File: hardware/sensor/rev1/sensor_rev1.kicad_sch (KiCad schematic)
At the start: 4 parts

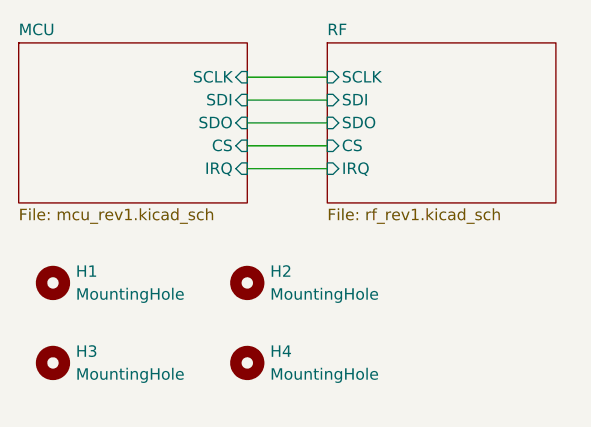
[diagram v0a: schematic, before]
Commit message: EG-49 Board size and mounting holes placed.
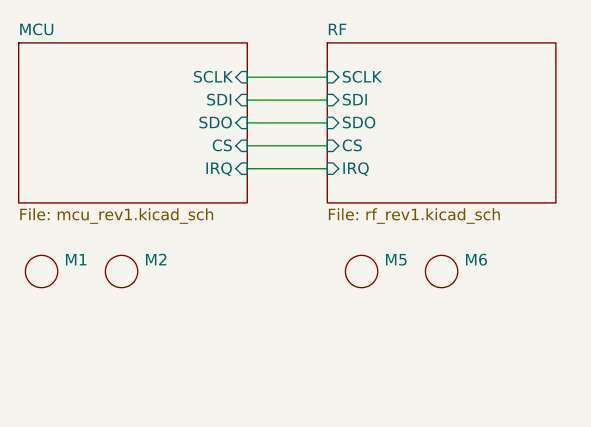
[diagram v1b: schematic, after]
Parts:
- removed H1, H2, H3, H4: MountingHole, MountingHole:MountingHole_2.5mm, symbol Mechanical:MountingHole
- added M1, M2, M5, M6: ~, MyParts:MountingHole_1.7mm, symbol MountingHole_1.7mm:MountingHole_1.7mm

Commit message: EG-49 ERC with no errors.
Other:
- title: Gateway -> Window Sensor
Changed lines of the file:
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@@
 	(paper "A4")
 	(title_block
-		(title "Gateway")
-		(date "2025-09-30")
-		(rev "RAV0.0")
+		(title "Window Sensor")
+		(date "2026-07-26")
+		(rev "REV1.0")
 		(company "NPX4U")
 	)

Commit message: EG-50 Fiducials included.
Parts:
- added FID1, FID2, FID3, FID4, FID5, FID6: Fiducial, Fiducial:Fiducial_1mm_Mask2mm, symbol Mechanical:Fiducial

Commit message: EG-70 All components in one face.
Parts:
- removed FID1, FID2, FID3: Fiducial, Fiducial:Fiducial_1mm_Mask2mm, symbol Mechanical:Fiducial
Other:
- moved on the sheet: FID4, FID5, FID6

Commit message: Connected the XTAL NC/GND pins to GND. Added a via for decouple capacitors of CC1101.
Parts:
- M1, M2, M5, M6: value ~ -> (none)
